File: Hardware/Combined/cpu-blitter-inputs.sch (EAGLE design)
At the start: 146 parts, among them IC1 74S08N, IC12 74S08N, IC16 7404N, IC18 7432N, IC20 7430N, IC21 7400N, IC3 74HC573N, IC31 7400N, IC32 7432N, IC4 7404N, IC5 7400N, IC53 7404N, IC54 74LS07N, IC7 74S08N, IC9 74LS74N, J2 TX25-40P-6ST-H1E, U1 W65C02SP, U2 VIA

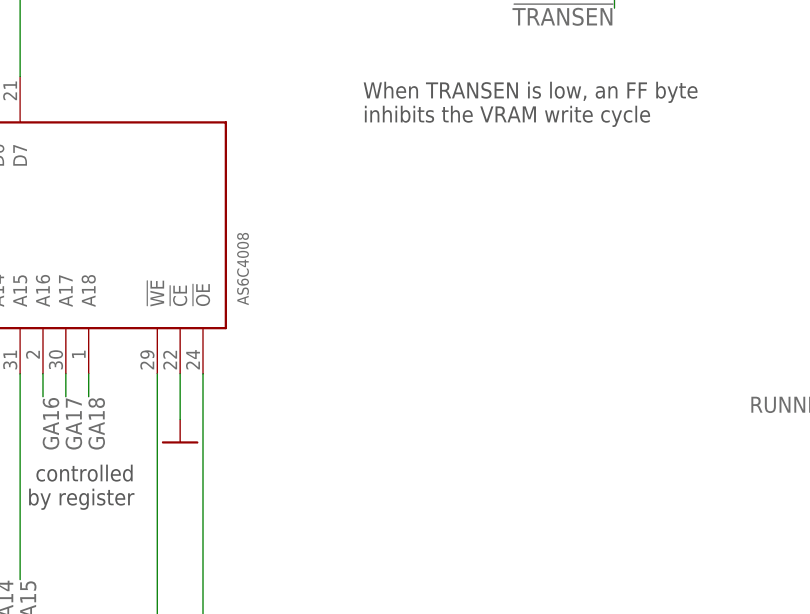
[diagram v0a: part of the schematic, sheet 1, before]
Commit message: add SMD oscillator to library and fix GRAM power connections
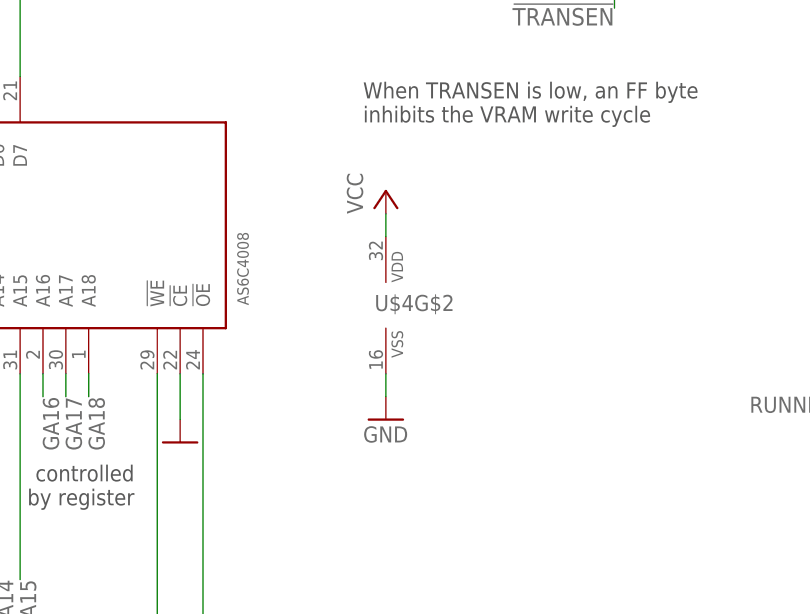
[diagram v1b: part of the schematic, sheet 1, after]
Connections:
- net GND: now also U$4G$2.VSS
- net VCC: now also U$4G$2.VDD
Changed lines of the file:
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@@
 <part name="GND34" library="supply1" library_urn="urn:adsk.eagle:library:371" deviceset="GND" device=""/>
 <part name="U$5" library="0_gametankparts" deviceset="SRAM_32K" device=""/>
+<part name="P+25" library="supply1" library_urn="urn:adsk.eagle:library:371" deviceset="VCC" device=""/>
+<part name="GND37" library="supply1" library_urn="urn:adsk.eagle:library:371" deviceset="GND" device=""/>
+<part name="P+28" library="supply1" library_urn="urn:adsk.eagle:library:371" deviceset="VCC" device=""/>
+<part name="GND44" library="supply1" library_urn="urn:adsk.eagle:library:371" deviceset="GND" device=""/>
 </parts>
 <sheets>
@@
 <attribute name="VALUE" x="124.46" y="111.76" size="1.778" layer="96"/>
 </instance>
+<instance part="U$4" gate="G$2" x="462.28" y="142.24" smashed="yes">
+<attribute name="NAME" x="461.01" y="141.605" size="1.778" layer="95"/>
+</instance>
+<instance part="P+28" gate="VCC" x="462.28" y="154.94" smashed="yes">
+<attribute name="VALUE" x="459.74" y="152.4" size="1.778" layer="96" rot="R90"/>
+</instance>
+<instance part="GND44" gate="1" x="462.28" y="129.54" smashed="yes">
+<attribute name="VALUE" x="459.74" y="127" size="1.778" layer="96"/>
+</instance>
 </instances>
 <busses>
@@
 <pinref part="GND34" gate="1" pin="GND"/>
 </segment>
+<segment>
+<pinref part="U$4" gate="G$2" pin="VSS"/>
+<pinref part="GND44" gate="1" pin="GND"/>
+<wire x1="462.28" y1="134.62" x2="462.28" y2="132.08" width="0.1524" layer="91"/>
+</segment>
 </net>
 <net name="VCC" class="0">
@@
 <wire x1="-403.86" y1="495.3" x2="-403.86" y2="492.76" width="0.1524" layer="91"/>
 </segment>
+<segment>
+<pinref part="P+28" gate="VCC" pin="VCC"/>
+<pinref part="U$4" gate="G$2" pin="VDD"/>
+<wire x1="462.28" y1="152.4" x2="462.28" y2="149.86" width="0.1524" layer="91"/>
+</segment>
 </net>
 <net name="N$15" class="0">
@@
 <attribute name="VALUE" x="33.02" y="45.72" size="1.778" layer="96"/>
 </instance>
+<instance part="P+25" gate="VCC" x="119.38" y="66.04" smashed="yes">
+<attribute name="VALUE" x="116.84" y="63.5" size="1.778" layer="96" rot="R90"/>
+</instance>
+<instance part="GND37" gate="1" x="119.38" y="40.64" smashed="yes">
+<attribute name="VALUE" x="116.84" y="38.1" size="1.778" layer="96"/>
+</instance>
 </instances>
 <busses>
@@
 <pinref part="GND5" gate="1" pin="GND"/>
 </segment>
+<segment>
+<pinref part="GND37" gate="1" pin="GND"/>
+<wire x1="119.38" y1="45.72" x2="119.38" y2="43.18" width="0.1524" layer="91"/>
+</segment>
 </net>
 <net name="VCC" class="0">
@@
 <pinref part="P+39" gate="VCC" pin="VCC"/>
 </segment>
+<segment>
+<pinref part="P+25" gate="VCC" pin="VCC"/>
+<wire x1="119.38" y1="63.5" x2="119.38" y2="60.96" width="0.1524" layer="91"/>
+</segment>
 </net>

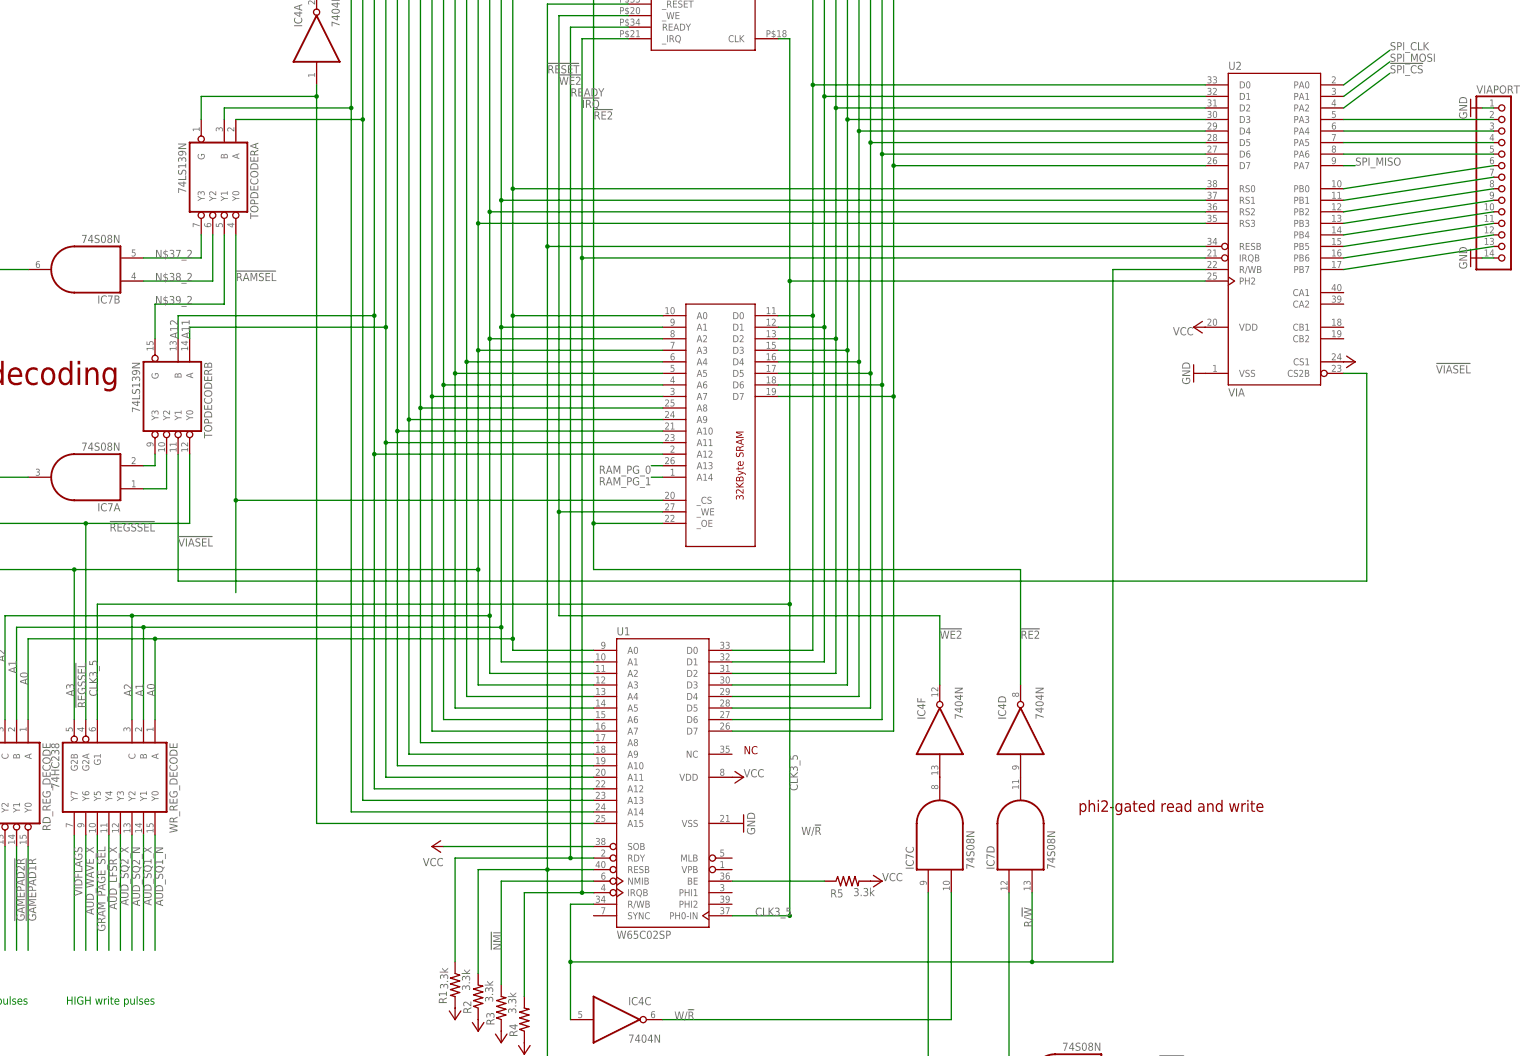
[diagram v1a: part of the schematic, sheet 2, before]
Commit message: fix ACP control lines (in schematic)
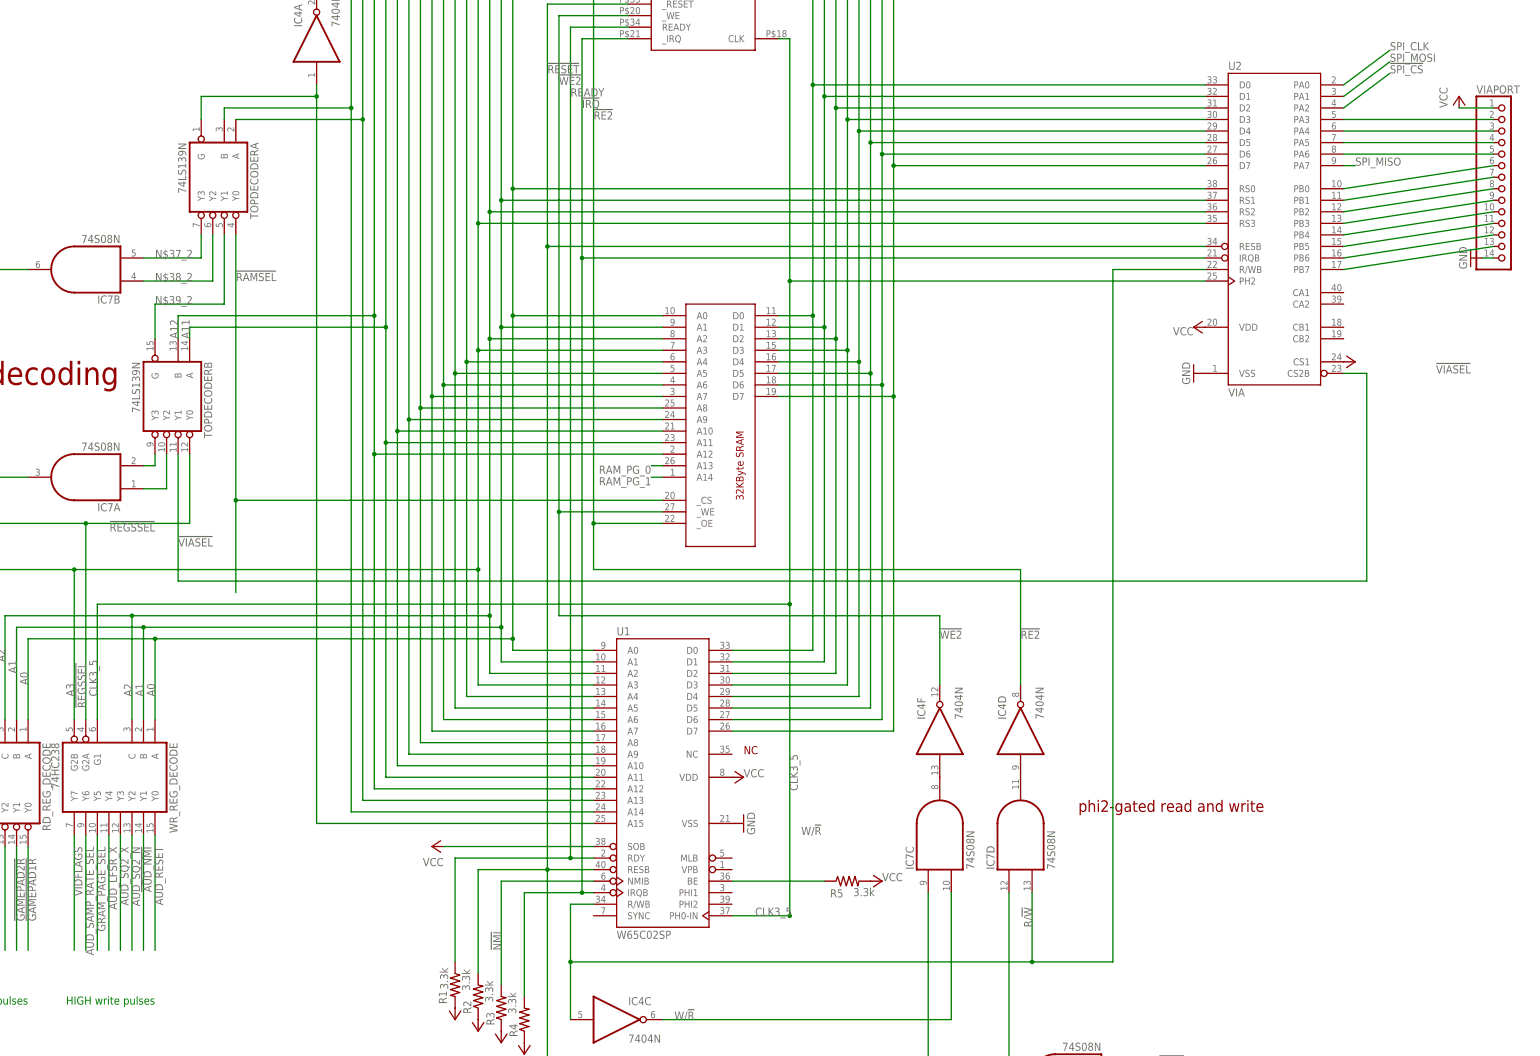
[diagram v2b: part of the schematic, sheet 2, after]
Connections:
- removed net AUD_SQ1_N: WR_REG_DECODEG$2.Y0
- removed net AUD_SQ1_X: WR_REG_DECODEG$2.Y1
- removed net AUD_WAVE_X: WR_REG_DECODEG$2.Y6
- net !AUD_NMI: now also WR_REG_DECODEG$2.Y1
- net AUD_RESET: now also WR_REG_DECODEG$2.Y0
- net AUD_SAMP_RATE_SEL: now also WR_REG_DECODEG$2.Y6
- net GND: no longer VIAPORT.1
- net VCC: now also VIAPORT.1
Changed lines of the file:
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@@
 <part name="C63" library="rcl" library_urn="urn:adsk.eagle:library:334" deviceset="C-US" device="025-024X044" package3d_urn="urn:adsk.eagle:package:23630/1" override_package3d_urn="urn:adsk.eagle:package:29285746/2" override_package_urn="urn:adsk.eagle:footprint:23136/1" value="0.1uF"/>
 <part name="VIAPORT" library="pinhead" library_urn="urn:adsk.eagle:library:325" deviceset="PINHD-1X14" device="" package3d_urn="urn:adsk.eagle:package:22417/2"/>
-<part name="GND45" library="supply1" library_urn="urn:adsk.eagle:library:371" deviceset="GND" device=""/>
 <part name="GND46" library="supply1" library_urn="urn:adsk.eagle:library:371" deviceset="GND" device=""/>
 <part name="U$6" library="0_gametankparts" deviceset="74HC163" device="" package3d_urn="urn:adsk.eagle:package:922/2"/>
@@
 <part name="P+28" library="supply1" library_urn="urn:adsk.eagle:library:371" deviceset="VCC" device=""/>
 <part name="GND44" library="supply1" library_urn="urn:adsk.eagle:library:371" deviceset="GND" device=""/>
+<part name="P+48" library="supply1" library_urn="urn:adsk.eagle:library:371" deviceset="VCC" device=""/>
 </parts>
 <sheets>
@@
 <attribute name="VALUE" x="232.41" y="165.1" size="1.778" layer="96"/>
 </instance>
-<instance part="GND45" gate="1" x="231.14" y="203.2" smashed="yes" rot="R270">
-<attribute name="VALUE" x="228.6" y="205.74" size="1.778" layer="96" rot="R270"/>
-</instance>
 <instance part="GND46" gate="1" x="231.14" y="170.18" smashed="yes" rot="R270">
 <attribute name="VALUE" x="228.6" y="172.72" size="1.778" layer="96" rot="R270"/>
@@
 </instance>
 <instance part="U$5" gate="G$1" x="66.04" y="134.62" smashed="yes"/>
+<instance part="P+48" gate="VCC" x="228.6" y="205.74" smashed="yes">
+<attribute name="VALUE" x="226.06" y="203.2" size="1.778" layer="96" rot="R90"/>
+</instance>
 </instances>
 <busses>
@@
 </segment>
 <segment>
-<pinref part="GND45" gate="1" pin="GND"/>
-<pinref part="VIAPORT" gate="A" pin="1"/>
-<wire x1="233.68" y1="203.2" x2="236.22" y2="203.2" width="0.1524" layer="91"/>
-</segment>
-<segment>
 <pinref part="GND46" gate="1" pin="GND"/>
 <pinref part="VIAPORT" gate="A" pin="14"/>
@@
 <pinref part="P+36" gate="VCC" pin="VCC"/>
 </segment>
+<segment>
+<pinref part="VIAPORT" gate="A" pin="1"/>
+<wire x1="228.6" y1="203.2" x2="236.22" y2="203.2" width="0.1524" layer="91"/>
+<pinref part="P+48" gate="VCC" pin="VCC"/>
+</segment>
 </net>
 <net name="!RAMSEL" class="0">
@@
 </segment>
 </net>
-<net name="AUD_SQ1_N" class="0">
+<net name="AUD_RESET" class="0">
 <segment>
 <pinref part="WR_REG_DECODE" gate="G$2" pin="Y0"/>
@@
 </segment>
 </net>
-<net name="AUD_SQ1_X" class="0">
+<net name="!AUD_NMI" class="0">
 <segment>
 <pinref part="WR_REG_DECODE" gate="G$2" pin="Y1"/>
@@
 </segment>
 </net>
-<net name="AUD_WAVE_X" class="0">
+<net name="AUD_SAMP_RATE_SEL" class="0">
 <segment>
 <pinref part="WR_REG_DECODE" gate="G$2" pin="Y6"/>

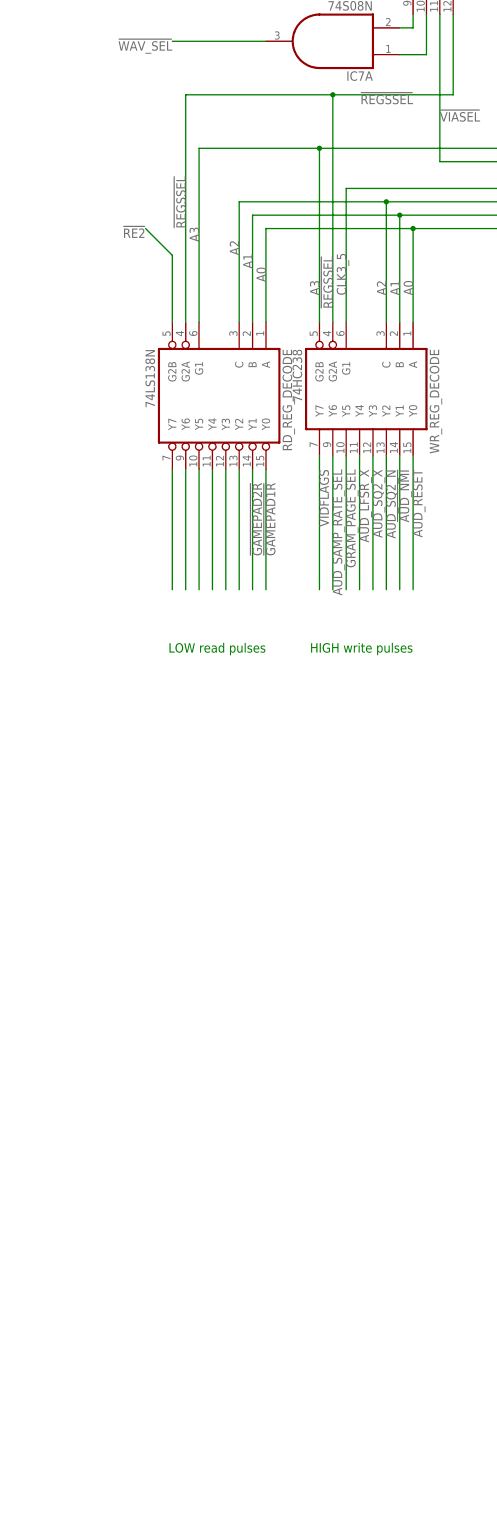
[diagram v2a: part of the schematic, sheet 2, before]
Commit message: Replace MUX for readregs with spare gates
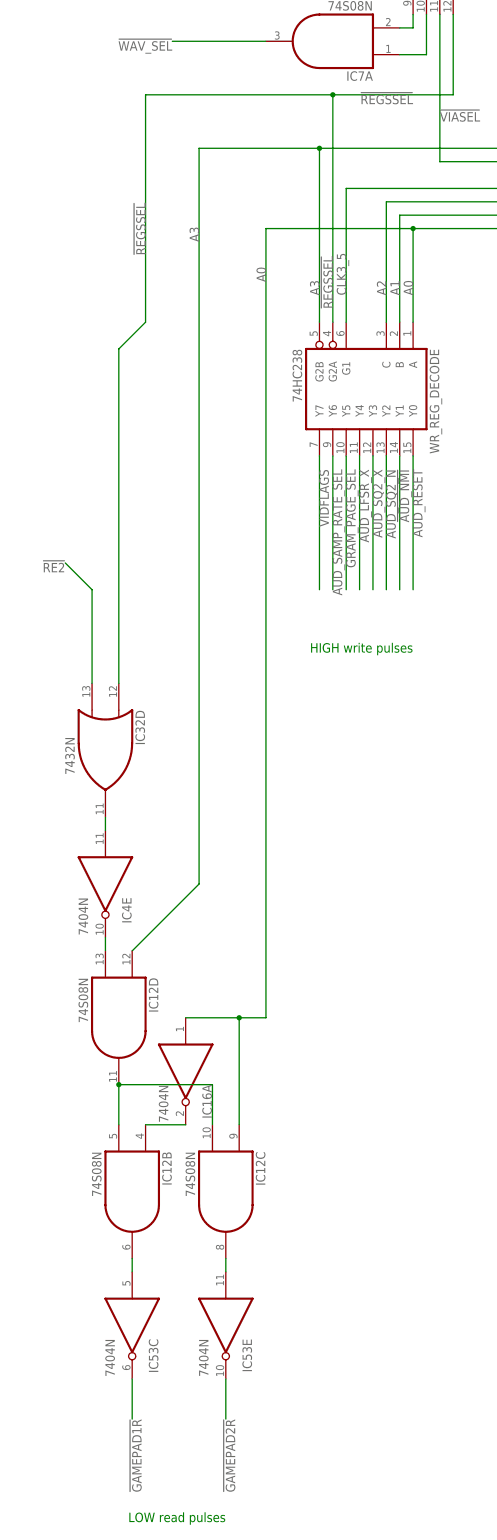
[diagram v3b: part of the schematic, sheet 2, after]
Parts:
- removed C37: (no value), rcl:C-US025-024X044
- removed RD_REG_DECODE: 74LS138N, 74xx-us:74LS138N
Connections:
- removed net N$91: RD_REG_DECODEA.Y2
- removed net N$92: RD_REG_DECODEA.Y3
- removed net N$93: RD_REG_DECODEA.Y4
- removed net N$95: RD_REG_DECODEA.Y5
- removed net N$97: RD_REG_DECODEA.Y6
- removed net N$99: RD_REG_DECODEA.Y7
- new net N$129: IC12B.O, IC53C.I
- new net N$149: IC12D.I1, IC4E.O
- new net N$152: IC32D.O, IC4E.I
- new net N$153: IC12B.I1, IC12C.I1, IC12D.O
- new net N$154: IC12B.I0, IC16A.O
- new net N$34: IC12C.O, IC53E.I
- net !GAMEPAD1R: now also IC53C.O; no longer RD_REG_DECODEA.Y0
- net !GAMEPAD2R: now also IC53E.O; no longer RD_REG_DECODEA.Y1
- net !RE2: now also IC32D.I1; no longer RD_REG_DECODEA.G2B
- net !REGSSEL: now also IC32D.I0; no longer RD_REG_DECODEA.G2A
- net A0: now also IC12C.I0, IC16A.I; no longer RD_REG_DECODEA.A
- net A1: no longer RD_REG_DECODEA.B
- net A2: no longer RD_REG_DECODEA.C
- net A3: now also IC12D.I0; no longer RD_REG_DECODEA.G1
- net GND: no longer C37.2
- net VCC: no longer C37.1
